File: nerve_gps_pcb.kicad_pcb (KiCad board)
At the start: 4 copper layers, 50 x 50 mm, 20 parts, among them J1 BF080-16-A-1-L-C, J2 WS2812B, J3 5V GPIO Breakout, U1 SAM-M10Q, U2 TXB0104QPWRQ1

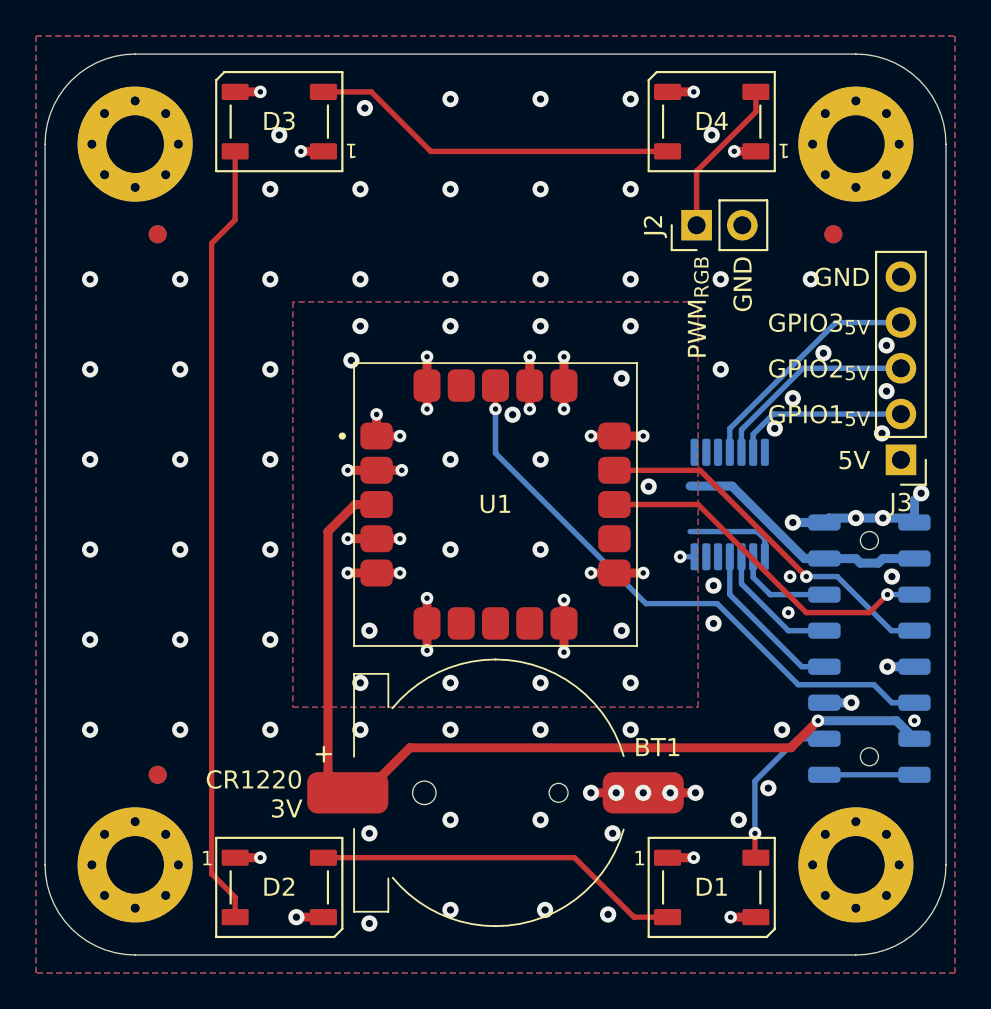
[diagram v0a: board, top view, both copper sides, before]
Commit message: Add minor decoupling caps
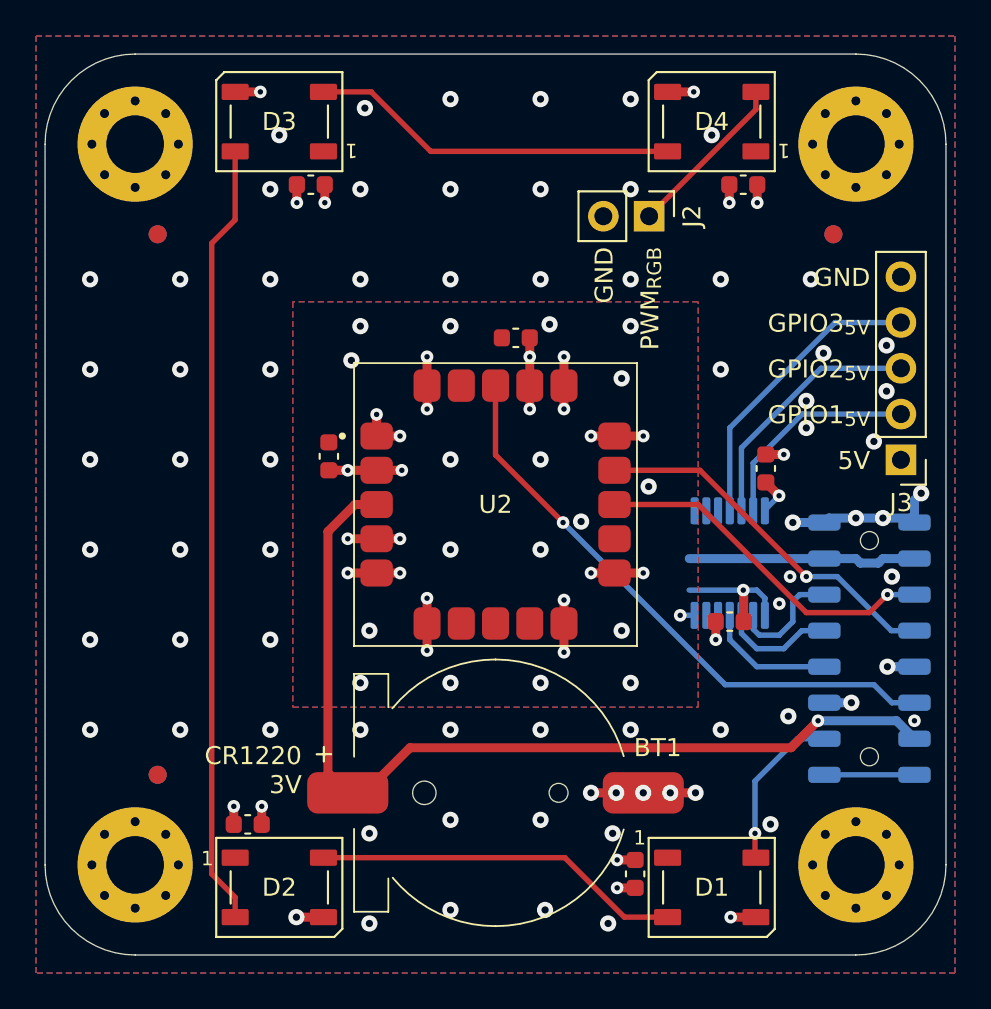
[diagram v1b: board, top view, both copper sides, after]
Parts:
- added C1: 100n, Capacitor_SMD:C_0603_1608Metric, F.Cu at (139.2, 102.3)
- added C2: 100n, Capacitor_SMD:C_0603_1608Metric, F.Cu at (149.6, 95.8)
- added C3: 100n, Capacitor_SMD:C_0603_1608Metric, F.Cu at (161.5, 111.5)
- added C4: 100n, Capacitor_SMD:C_0603_1608Metric, F.Cu at (163.5, 103.0)
- added C5: 100n, Capacitor_SMD:C_0603_1608Metric, F.Cu at (156.2, 125.5)
- added C6: 100n, Capacitor_SMD:C_0603_1608Metric, F.Cu at (134.8, 122.8)
- added C7: 100n, Capacitor_SMD:C_0603_1608Metric, F.Cu at (138.2, 87.2)
- added C8: 100n, Capacitor_SMD:C_0603_1608Metric, F.Cu at (162.2, 87.2)
- moved U1 3.25 mm to (161.5, 108.2)
- moved J2 2.68 mm to (157.0, 89.0), turned to -90 degrees
- renumbered U2 to U1, U1 to U2
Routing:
- net GND: track 41.0 -> 47.0 mm, vias 111 -> 115
- net /GPIO_3_{5V}: track 13.2 -> 16.5 mm
- net /GPIO_2_{5V}: track 11.5 -> 14.2 mm
- net /GPIO_1_{5V}: track 9.66 -> 12.0 mm
- net +3V3: track 25.5 -> 27.8 mm, vias 4 -> 5
- net /GPIO_3: track 9.01 -> 7.22 mm
- net /GPIO_1: track 5.49 -> 6.44 mm
- net +5V: track 14.0 -> 14.9 mm, vias 8 -> 9
- net /GPIO_2: track 7.18 -> 6.37 mm
- net Net-(D4-DOUT): track 8.76 -> 9.35 mm

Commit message: Add CR1220 reverse polarity schottky diode
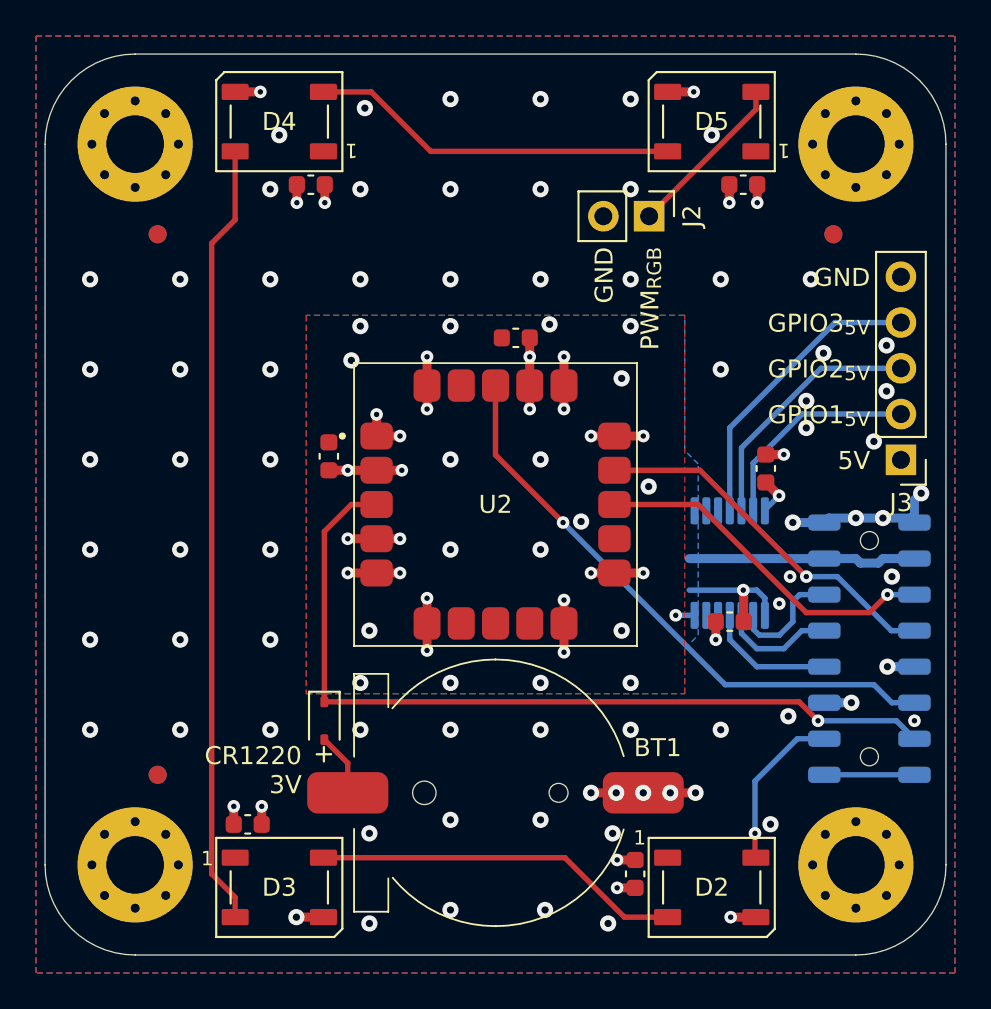
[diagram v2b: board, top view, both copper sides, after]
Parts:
- added D1: RB751V-40, Diode_SMD:D_SOD-323, F.Cu at (139.0, 117.0)
- renumbered D1 to D2, D2 to D3, D3 to D4, D4 to D5
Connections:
- BT1 pad 2: +3VBATT -> Net-(D1-A)
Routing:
- net +3VBATT: track 51.8 -> 46.6 mm
- net Net-(D1-A): track 0.00 -> 3.49 mm

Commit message: Cleanup and fix outer layer non-functional pads
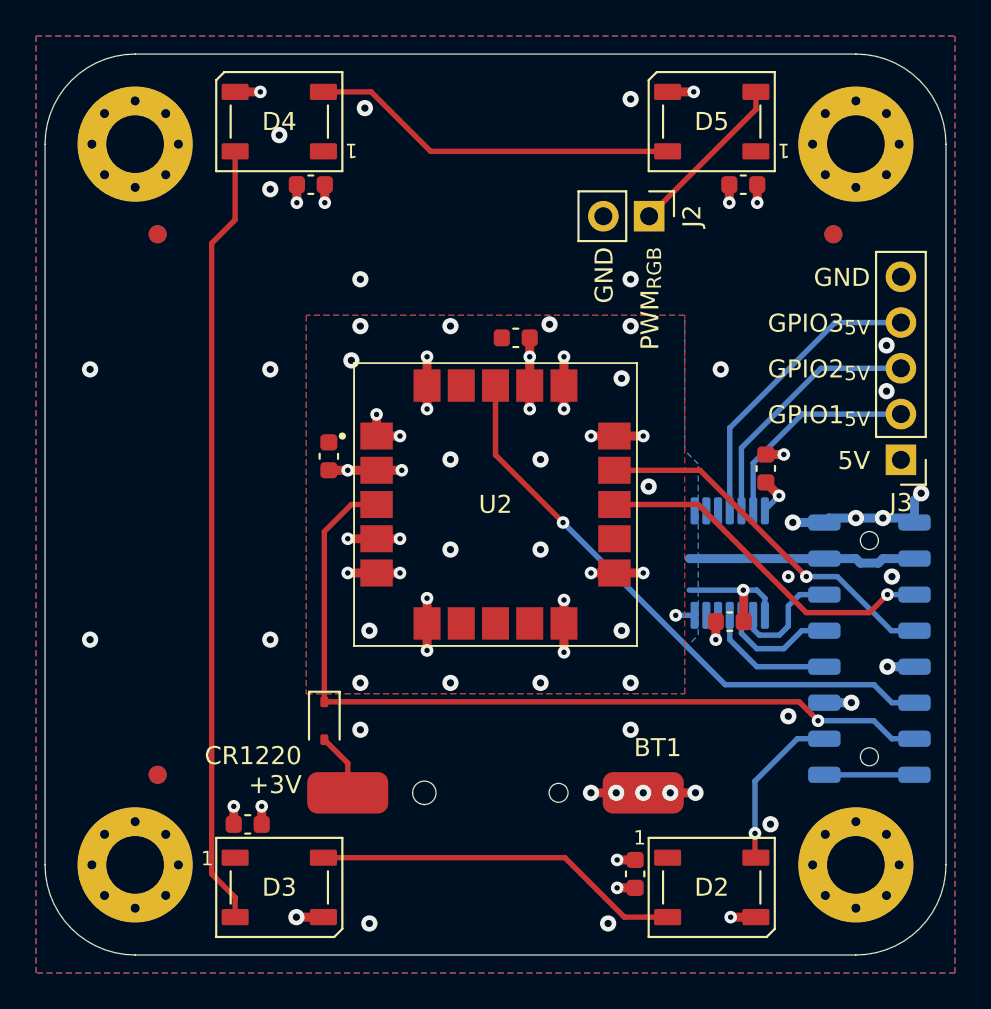
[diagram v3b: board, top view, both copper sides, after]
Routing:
- net GND: vias 115 -> 74
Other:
- board text added: "CR1220 +3V"
- board text removed: "CR1220 3V"

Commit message: Remove CR1220 schottky diode
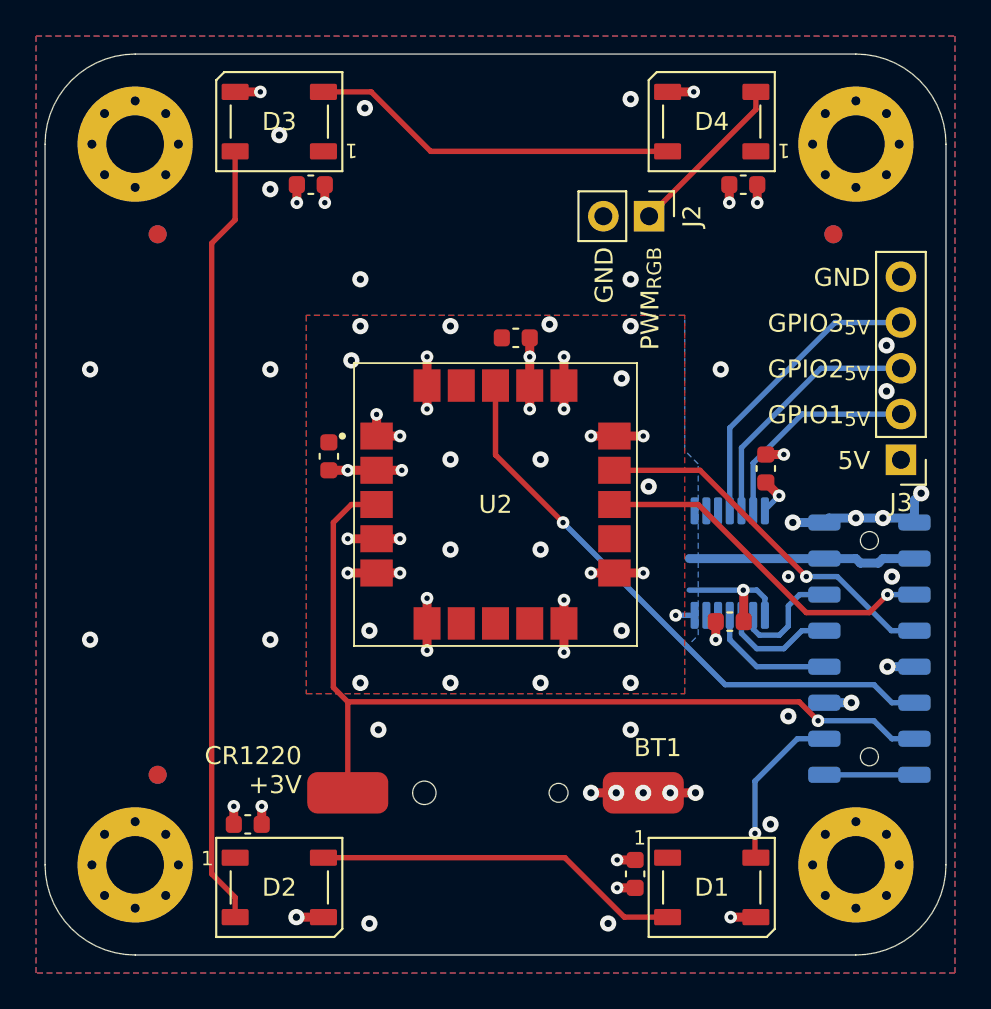
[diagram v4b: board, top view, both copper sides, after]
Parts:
- removed the D1 at (139.0, 117.0)
- renumbered D2 to D1, D3 to D2, D4 to D3, D5 to D4
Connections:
- BT1 pad 2: Net-(D1-A) -> +3VBATT
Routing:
- net +3VBATT: track 46.6 -> 50.4 mm
- net Net-(D1-A): track 3.49 -> 0.00 mm
